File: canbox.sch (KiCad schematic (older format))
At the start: 3 parts

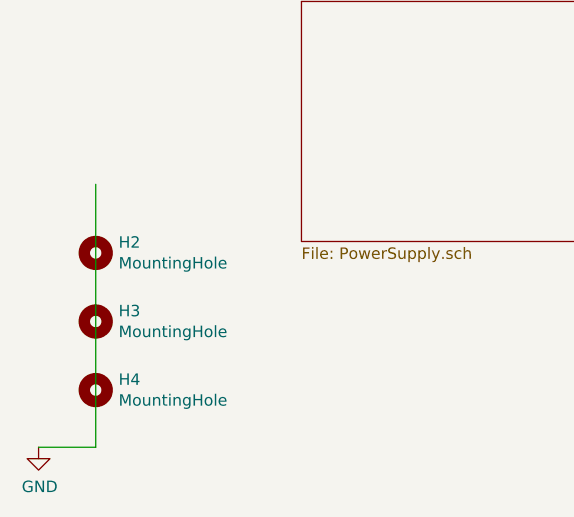
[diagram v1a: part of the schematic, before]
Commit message: V3 bigger board, RMII instrumentation, inverter
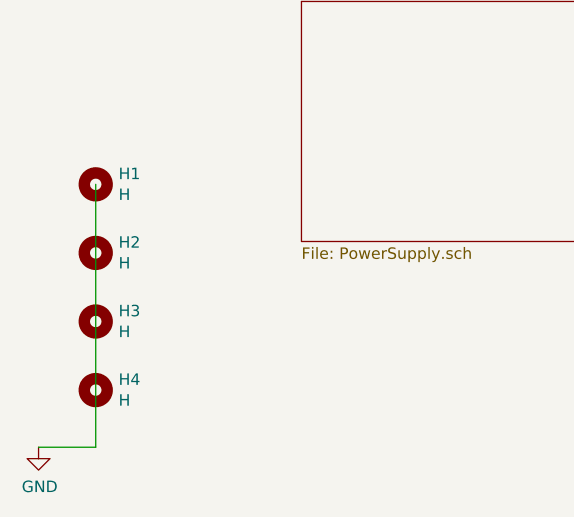
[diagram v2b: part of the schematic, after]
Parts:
- added H1: H, MountingHole:MountingHole_2.5mm_Pad_Via, symbol canbox-rescue:MountingHole-Mechanical
- H2, H3, H4: value MountingHole -> H
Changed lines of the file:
@@
-EESchema Schematic File Version 4
+EESchema Schematic File Version 5
 LIBS:canbox-cache
-EELAYER 29 0
+EELAYER 30 0
 EELAYER END
 $Descr A4 11693 8268
@@
 Comment3 ""
 Comment4 ""
+Comment5 ""
+Comment6 ""
+Comment7 ""
+Comment8 ""
+Comment9 ""
 $EndDescr
 $Sheet
@@
 P 1850 5950
 F 0 "H4" H 1950 5996 50  0000 L CNN
-F 1 "MountingHole" H 1950 5905 50  0000 L CNN
+F 1 "H" H 1950 5905 50  0000 L CNN
 F 2 "MountingHole:MountingHole_2.5mm_Pad_Via" H 1850 5950 50  0001 C CNN
 F 3 "~" H 1850 5950 50  0001 C CNN
@@
 P 1850 5650
 F 0 "H3" H 1950 5696 50  0000 L CNN
-F 1 "MountingHole" H 1950 5605 50  0000 L CNN
+F 1 "H" H 1950 5605 50  0000 L CNN
 F 2 "MountingHole:MountingHole_2.5mm_Pad_Via" H 1850 5650 50  0001 C CNN
 F 3 "~" H 1850 5650 50  0001 C CNN
@@
 P 1850 5350
 F 0 "H2" H 1950 5396 50  0000 L CNN
-F 1 "MountingHole" H 1950 5305 50  0000 L CNN
+F 1 "H" H 1950 5305 50  0000 L CNN
 F 2 "MountingHole:MountingHole_2.5mm_Pad_Via" H 1850 5350 50  0001 C CNN
 F 3 "~" H 1850 5350 50  0001 C CNN
@@
 Wire Wire Line
 	1850 6200 1600 6200
+$Comp
+L canbox-rescue:MountingHole-Mechanical H1
+U 1 1 5F0144FA
+P 1850 5050
+F 0 "H1" H 1950 5096 50  0000 L CNN
+F 1 "H" H 1950 5005 50  0000 L CNN
+F 2 "MountingHole:MountingHole_2.5mm_Pad_Via" H 1850 5050 50  0001 C CNN
+F 3 "~" H 1850 5050 50  0001 C CNN
+	1    1850 5050
+	1    0    0    -1
+$EndComp
 $EndSCHEMATC

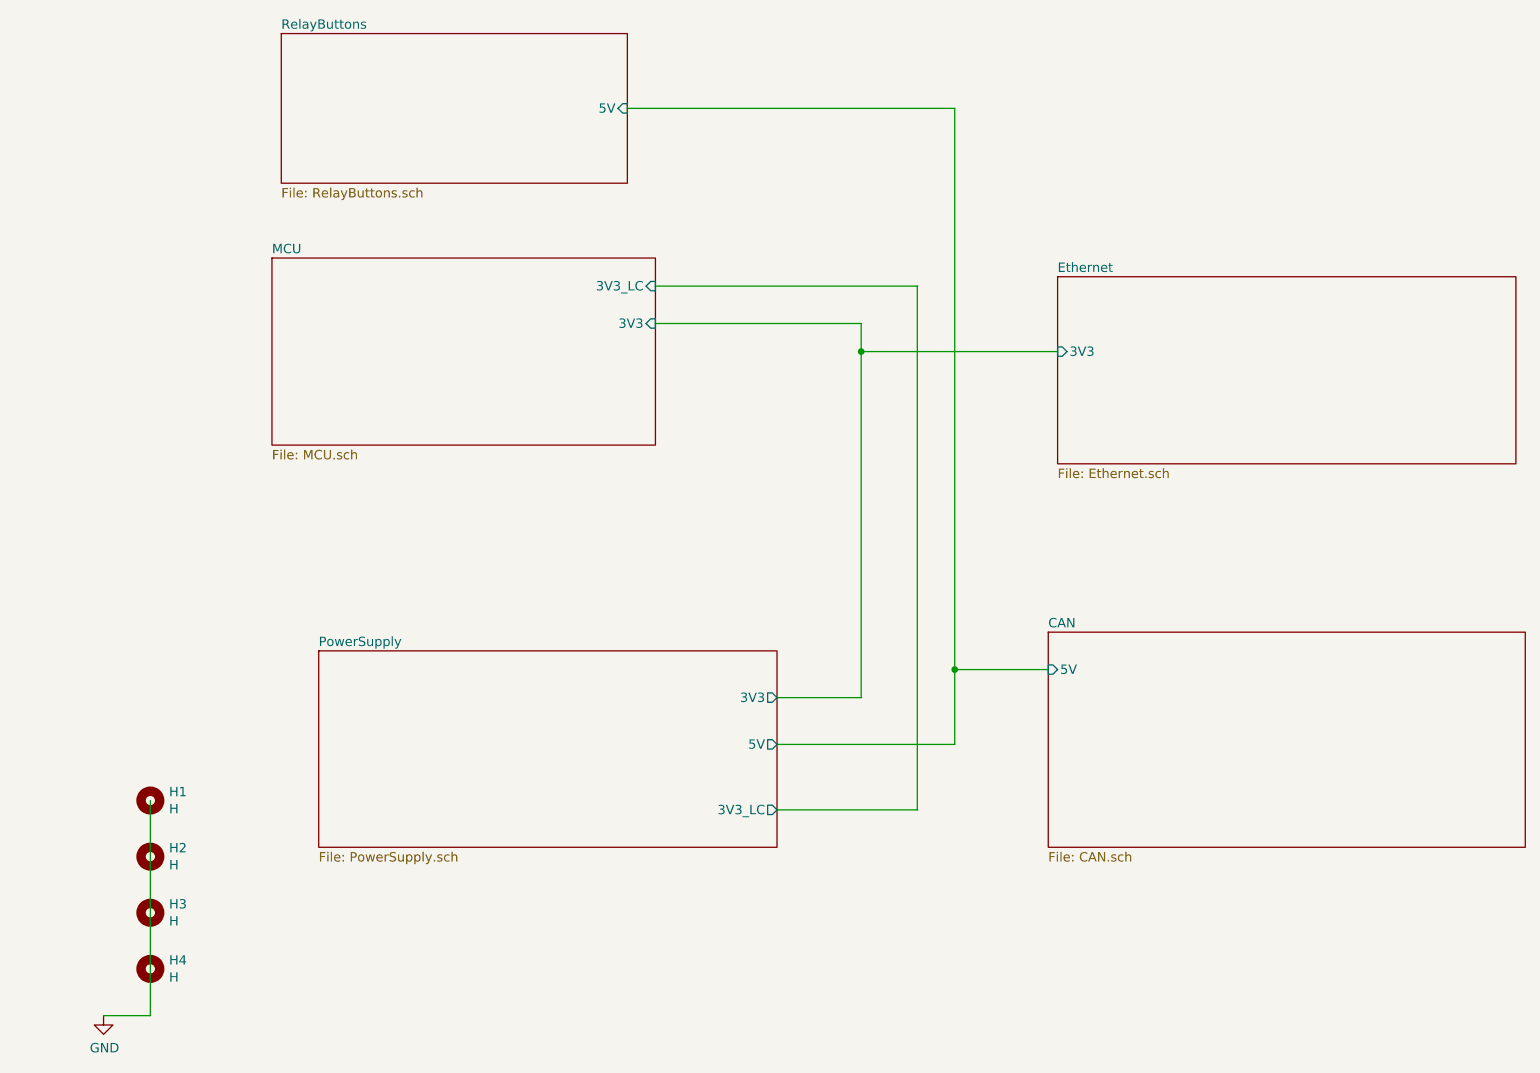
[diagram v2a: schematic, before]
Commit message: Switch to 4 Layer PCB as the RMII loopback doesn't work
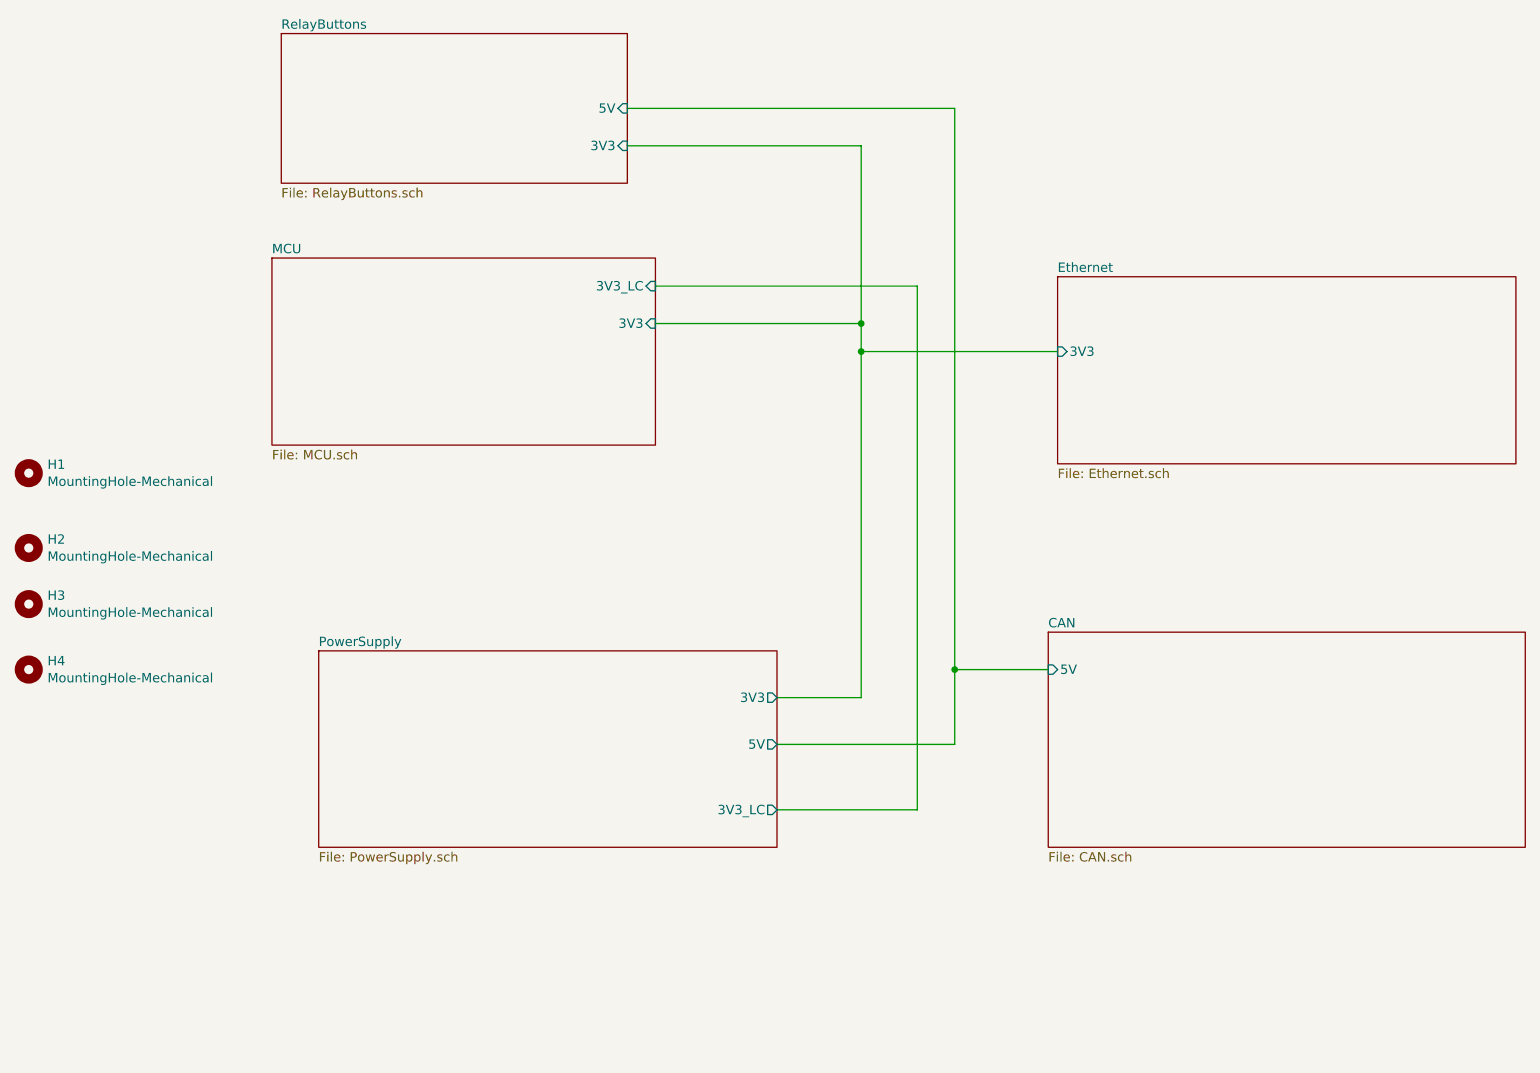
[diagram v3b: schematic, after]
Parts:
- H1, H2, H3, H4: value H -> MountingHole-Mechanical; footprint MountingHole:MountingHole_2.5mm_Pad_Via -> MountingHole:MountingHole_2.2mm_M2_DIN965
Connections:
- net labels removed: GND
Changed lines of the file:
@@
 F1 "RelayButtons.sch" 50
 F2 "5V" I R 4400 1350 50
+F3 "3V3" I R 4400 1550 50
 $EndSheet
 Wire Wire Line
@@
 	5950 2300 4550 2300
 $Comp
-L canbox-rescue:MountingHole-Mechanical H4
-U 1 1 5C0741C7
-P 1850 5950
-F 0 "H4" H 1950 5996 50  0000 L CNN
-F 1 "H" H 1950 5905 50  0000 L CNN
-F 2 "MountingHole:MountingHole_2.5mm_Pad_Via" H 1850 5950 50  0001 C CNN
-F 3 "~" H 1850 5950 50  0001 C CNN
-	1    1850 5950
+L canbox-rescue:MountingHole-Mechanical H1
+U 1 1 5E0AFF15
+P 1200 3300
+F 0 "H1" H 1300 3346 50  0000 L CNN
+F 1 "MountingHole-Mechanical" H 1300 3255 50  0000 L CNN
+F 2 "MountingHole:MountingHole_2.2mm_M2_DIN965" H 1200 3300 50  0001 C CNN
+F 3 "" H 1200 3300 50  0001 C CNN
+	1    1200 3300
+	1    0    0    -1
+$EndComp
+$Comp
+L canbox-rescue:MountingHole-Mechanical H2
+U 1 1 5E0B01F5
+P 1200 3700
+F 0 "H2" H 1300 3746 50  0000 L CNN
+F 1 "MountingHole-Mechanical" H 1300 3655 50  0000 L CNN
+F 2 "MountingHole:MountingHole_2.2mm_M2_DIN965" H 1200 3700 50  0001 C CNN
+F 3 "" H 1200 3700 50  0001 C CNN
+	1    1200 3700
 	1    0    0    -1
 $EndComp
 $Comp
 L canbox-rescue:MountingHole-Mechanical H3
-U 1 1 5C07437F
-P 1850 5650
-F 0 "H3" H 1950 5696 50  0000 L CNN
-F 1 "H" H 1950 5605 50  0000 L CNN
-F 2 "MountingHole:MountingHole_2.5mm_Pad_Via" H 1850 5650 50  0001 C CNN
-F 3 "~" H 1850 5650 50  0001 C CNN
-	1    1850 5650
+U 1 1 5E0B036E
+P 1200 4000
+F 0 "H3" H 1300 4046 50  0000 L CNN
+F 1 "MountingHole-Mechanical" H 1300 3955 50  0000 L CNN
+F 2 "MountingHole:MountingHole_2.2mm_M2_DIN965" H 1200 4000 50  0001 C CNN
+F 3 "" H 1200 4000 50  0001 C CNN
+	1    1200 4000
 	1    0    0    -1
 $EndComp
 $Comp
-L canbox-rescue:MountingHole-Mechanical H2
-U 1 1 5C074496
-P 1850 5350
-F 0 "H2" H 1950 5396 50  0000 L CNN
-F 1 "H" H 1950 5305 50  0000 L CNN
-F 2 "MountingHole:MountingHole_2.5mm_Pad_Via" H 1850 5350 50  0001 C CNN
-F 3 "~" H 1850 5350 50  0001 C CNN
-	1    1850 5350
-	1    0    0    -1
-$EndComp
-$Comp
-L canbox-rescue:GND-power #PWR0104
-U 1 1 5C074F1C
-P 1600 6200
-F 0 "#PWR0104" H 1600 5950 50  0001 C CNN
-F 1 "GND" H 1605 6027 50  0000 C CNN
-F 2 "" H 1600 6200 50  0001 C CNN
-F 3 "" H 1600 6200 50  0001 C CNN
-	1    1600 6200
+L canbox-rescue:MountingHole-Mechanical H4
+U 1 1 5E0B05BD
+P 1200 4350
+F 0 "H4" H 1300 4396 50  0000 L CNN
+F 1 "MountingHole-Mechanical" H 1300 4305 50  0000 L CNN
+F 2 "MountingHole:MountingHole_2.2mm_M2_DIN965" H 1200 4350 50  0001 C CNN
+F 3 "" H 1200 4350 50  0001 C CNN
+	1    1200 4350
 	1    0    0    -1
 $EndComp
 Wire Wire Line
-	1850 5050 1850 6200
+	4400 1550 5650 1550
 Wire Wire Line
-	1850 6200 1600 6200
-$Comp
-L canbox-rescue:MountingHole-Mechanical H1
-U 1 1 5F0144FA
-P 1850 5050
-F 0 "H1" H 1950 5096 50  0000 L CNN
-F 1 "H" H 1950 5005 50  0000 L CNN
-F 2 "MountingHole:MountingHole_2.5mm_Pad_Via" H 1850 5050 50  0001 C CNN
-F 3 "~" H 1850 5050 50  0001 C CNN
-	1    1850 5050
-	1    0    0    -1
-$EndComp
+	5650 1550 5650 2500
+Connection ~ 5650 2500
 $EndSCHEMATC

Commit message: V5 now impedance controlled
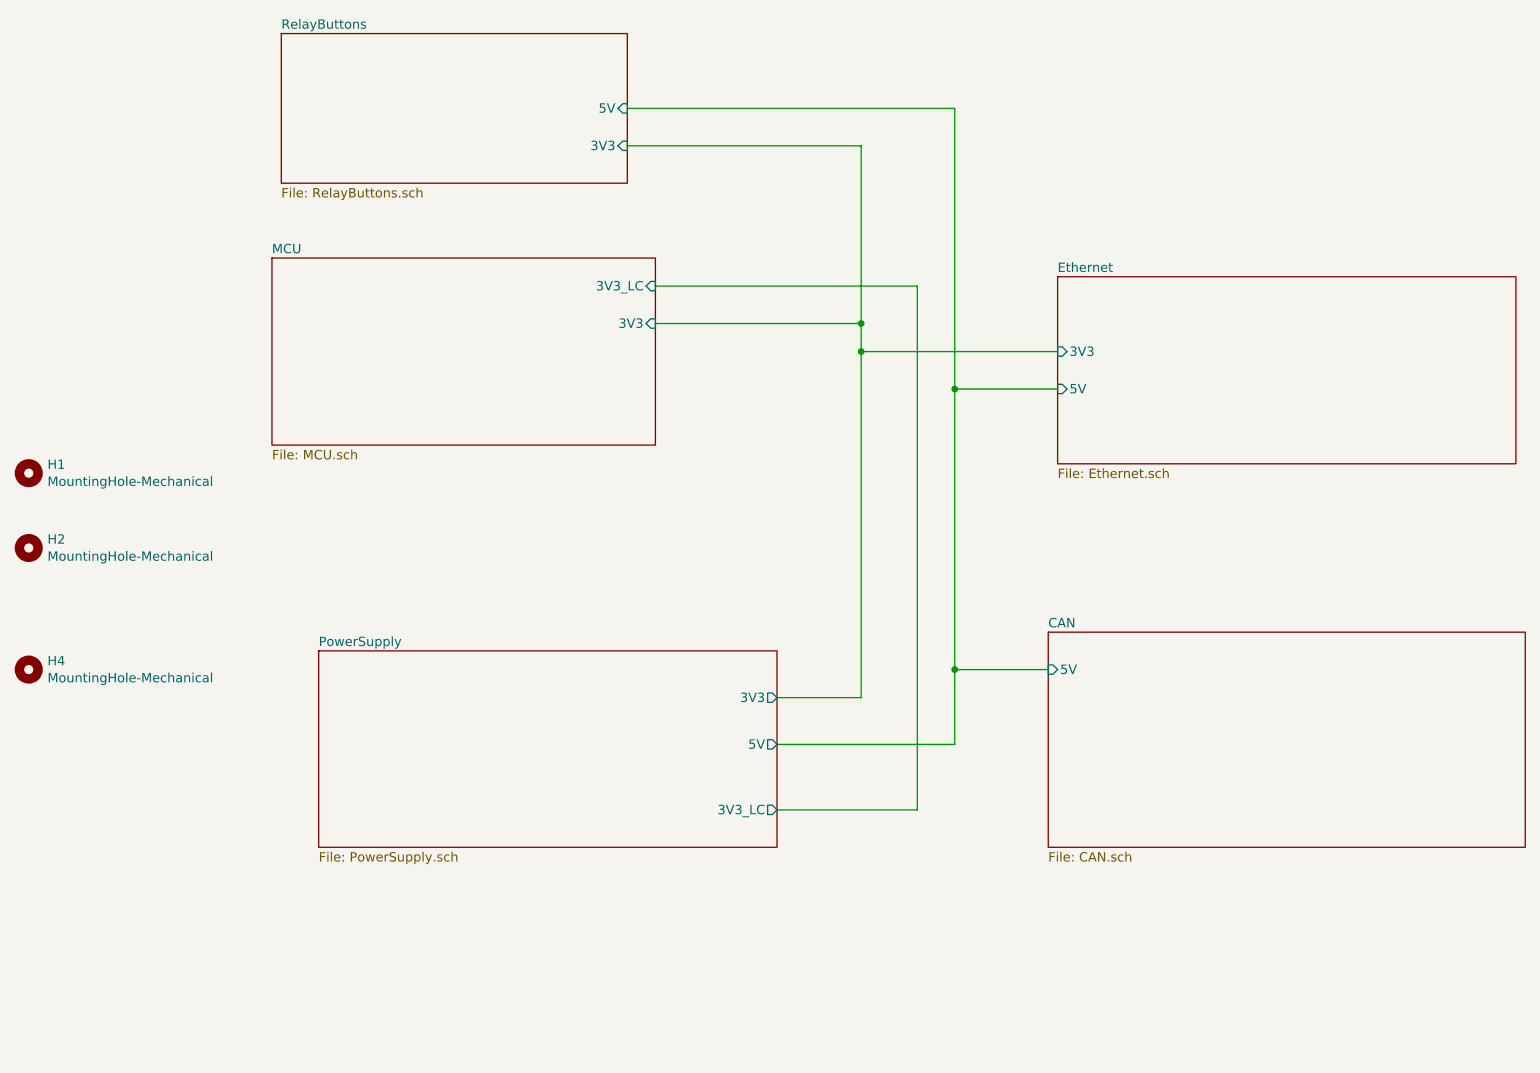
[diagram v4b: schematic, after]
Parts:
- removed H3: MountingHole-Mechanical, MountingHole:MountingHole_2.2mm_M2_DIN965, symbol canbox-rescue:MountingHole-Mechanical
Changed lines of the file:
@@
 F1 "Ethernet.sch" 50
 F2 "3V3" I L 6700 2650 50
+F3 "5V" I L 6700 2850 50
 $EndSheet
 $Sheet
@@
 $EndSheet
 Wire Wire Line
-	6150 4350 6150 1350
+	6150 4350 6150 2850
 Wire Wire Line
 	6150 1350 4400 1350
@@
 Wire Wire Line
 	5200 5100 5950 5100
-Wire Wire Line
-	5950 5100 5950 2300
 Wire Wire Line
 	5950 2300 4550 2300
@@
 $EndComp
 $Comp
-L canbox-rescue:MountingHole-Mechanical H3
-U 1 1 5E0B036E
-P 1200 4000
-F 0 "H3" H 1300 4046 50  0000 L CNN
-F 1 "MountingHole-Mechanical" H 1300 3955 50  0000 L CNN
-F 2 "MountingHole:MountingHole_2.2mm_M2_DIN965" H 1200 4000 50  0001 C CNN
-F 3 "" H 1200 4000 50  0001 C CNN
-	1    1200 4000
-	1    0    0    -1
-$EndComp
-$Comp
 L canbox-rescue:MountingHole-Mechanical H4
 U 1 1 5E0B05BD
@@
 	5650 1550 5650 2500
 Connection ~ 5650 2500
+Wire Wire Line
+	5950 2300 5950 5100
+Wire Wire Line
+	6700 2850 6150 2850
+Connection ~ 6150 2850
+Wire Wire Line
+	6150 2850 6150 1350
 $EndSCHEMATC
